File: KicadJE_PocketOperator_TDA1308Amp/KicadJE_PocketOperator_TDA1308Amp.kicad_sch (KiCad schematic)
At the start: 7 parts, among them J101 AudioJack3, J102 AudioJack3, J103 AudioJack3, J104 AudioJack3, J105 AudioJack3, J106 AudioJack3

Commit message: battery power
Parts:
- added C101: C, symbol Device:C
- added SW101: SW_SPST, symbol Switch:SW_SPST
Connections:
- net +BATT: now reaches BT101.1 (+)
- net +BATT: now also C101.1, SW101.1 (A)
- net GND: now reaches BT101.2 (-)
- net GND: now also J101.S, J102.S, J103.S, J104.S, J105.S, J106.S, C101.2
- net Out2R: now reaches J105.R
- net Out2L: now reaches J105.T
- net Out1R: now reaches J104.R
- net Out1L: now reaches J104.T
- net Out3R: now reaches J106.R
- net Out3L: now reaches J106.T
- new net +3V8: SW101.2 (B)
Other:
- moved on the sheet: BT101

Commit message: TDA1308 footprint
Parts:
- added C102: 10u, Resistor_SMD:R_0805_2012Metric_Pad1.20x1.40mm_HandSolder, symbol Device:C
- added D101: LED, LED_SMD:LED_0805_2012Metric_Pad1.15x1.40mm_HandSolder, symbol Device:LED
- added R101: 1k, Resistor_SMD:R_0805_2012Metric_Pad1.20x1.40mm_HandSolder, symbol Device:R
- BT101: footprint (none) -> Battery:BatteryHolder_Keystone_2460_1xAA
- C101: value C -> 1u
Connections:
- net +3V8: now also R101.1
- net GND: now also D101.1 (K)
- new net: D101.2 (A), R101.2

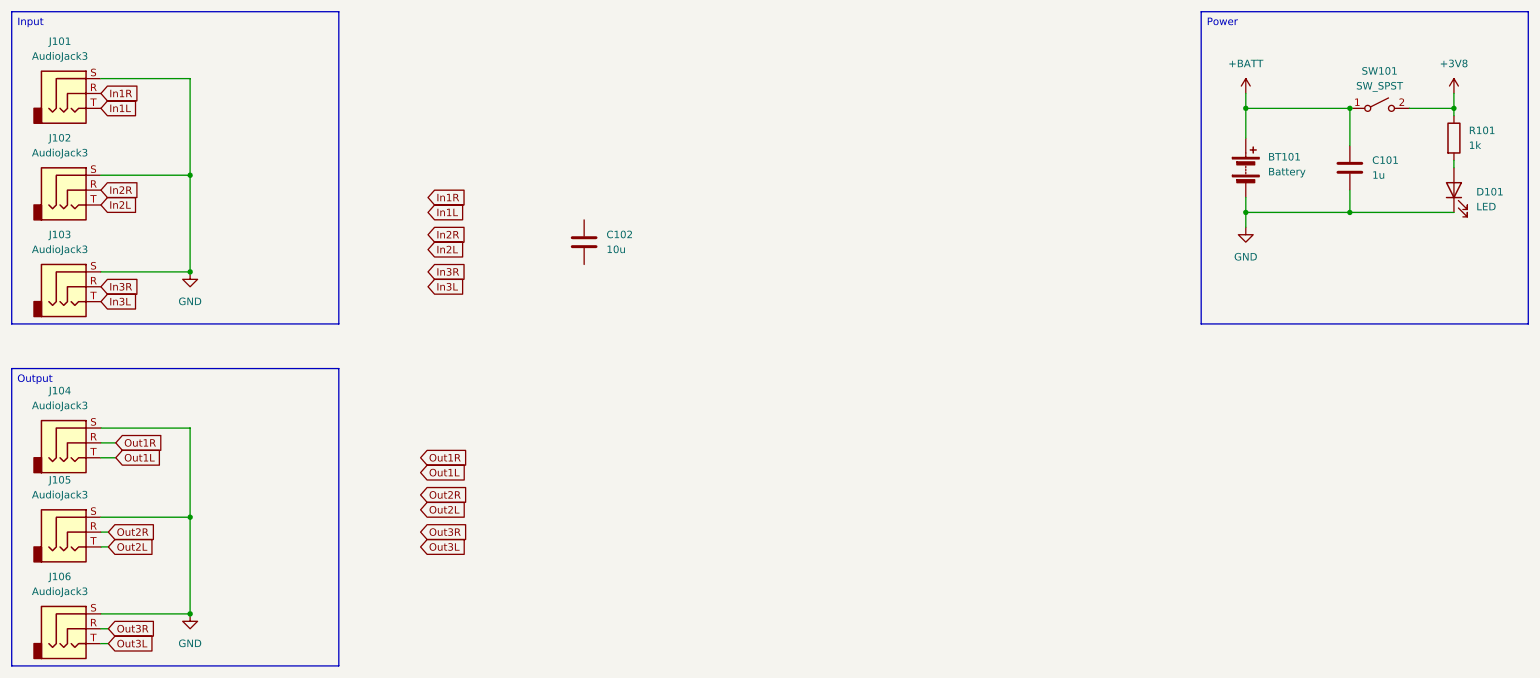
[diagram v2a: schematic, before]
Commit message: TDA1308 symbol
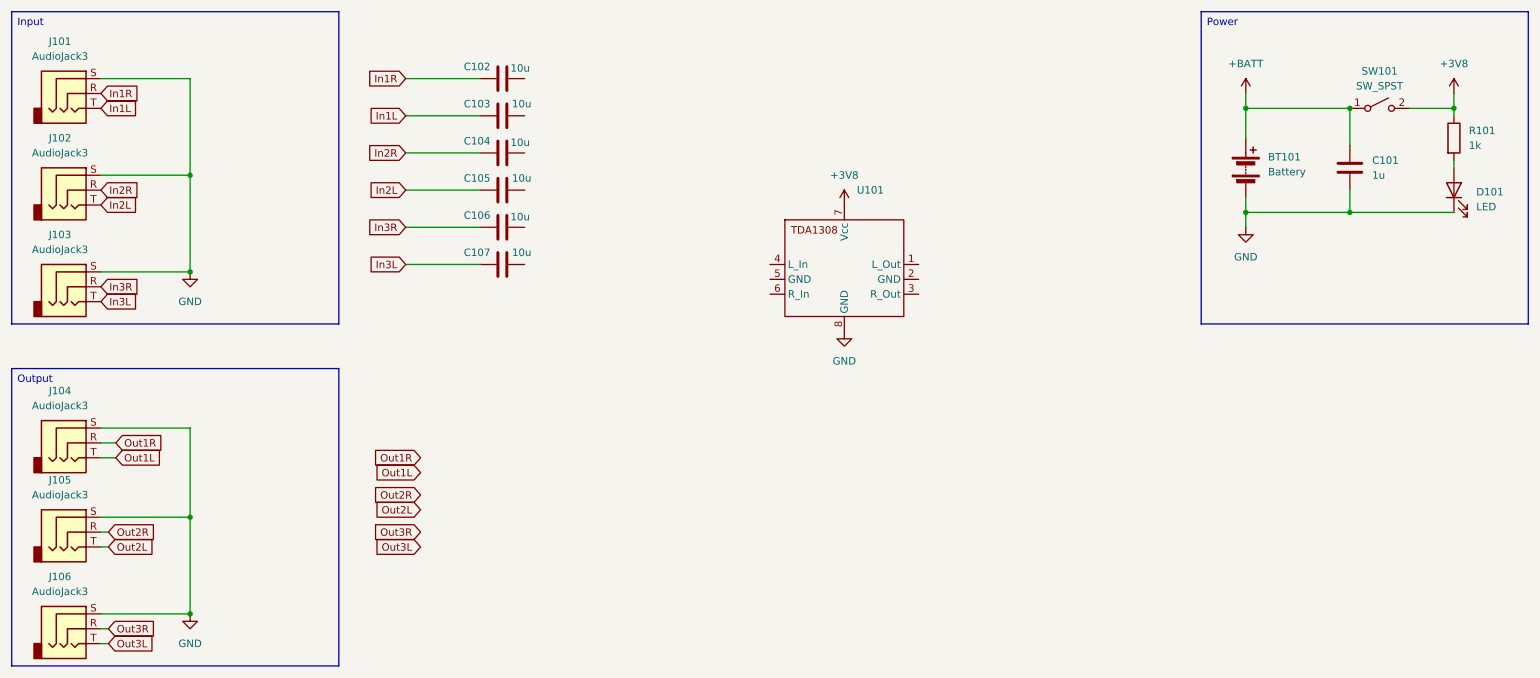
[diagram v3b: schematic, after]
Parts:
- added C103, C104, C105, C106, C107: 10u, Resistor_SMD:R_0805_2012Metric_Pad1.20x1.40mm_HandSolder, symbol Device:C
- added U101: ~, AJ_2025_Library:TDA1308_PCB, symbol AJ_2025:TDA_1308_PCB
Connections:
- net +3V8: now also U101.7 (Vcc)
- net GND: now also U101.8 (GND)
- net In1L: now also C103.1
- net In1R: now also C102.1
- net In2L: now also C105.1
- net In2R: now also C104.1
- net In3L: now also C107.1
- net In3R: now also C106.1
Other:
- moved on the sheet: C102

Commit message: Footprints Updated
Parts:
- added JP101: Out2R, Jumper:SolderJumper-2_P1.3mm_Bridged_RoundedPad1.0x1.5mm, symbol Jumper:Jumper_2_Bridged
- added JP102: Out2L, Jumper:SolderJumper-2_P1.3mm_Bridged_RoundedPad1.0x1.5mm, symbol Jumper:Jumper_2_Bridged
- added JP103: Out3R, Jumper:SolderJumper-2_P1.3mm_Bridged_RoundedPad1.0x1.5mm, symbol Jumper:Jumper_2_Bridged
- added JP104: Out3L, Jumper:SolderJumper-2_P1.3mm_Bridged_RoundedPad1.0x1.5mm, symbol Jumper:Jumper_2_Bridged
- added JP105: InL, Jumper:SolderJumper-2_P1.3mm_Open_RoundedPad1.0x1.5mm, symbol Jumper:Jumper_2_Open
- added JP106: InR, Jumper:SolderJumper-2_P1.3mm_Open_RoundedPad1.0x1.5mm, symbol Jumper:Jumper_2_Open
- added R102, R103, R104, R105, R106, R107: 10k, Resistor_SMD:R_0805_2012Metric_Pad1.20x1.40mm_HandSolder, symbol Device:R
- C101: footprint (none) -> Capacitor_SMD:C_0805_2012Metric_Pad1.18x1.45mm_HandSolder
- J101: value AudioJack3 -> In 1 + Sync; footprint (none) -> Connector_Audio:Jack_3.5mm_PJ311_Horizontal
- J102: value AudioJack3 -> In 2; footprint (none) -> Connector_Audio:Jack_3.5mm_PJ311_Horizontal
- J103: value AudioJack3 -> In 3; footprint (none) -> Connector_Audio:Jack_3.5mm_PJ311_Horizontal
- J104: value AudioJack3 -> Out Stereo; footprint (none) -> Connector_Audio:Jack_3.5mm_PJ311_Horizontal
- J105: value AudioJack3 -> Sync1; footprint (none) -> Connector_Audio:Jack_3.5mm_PJ311_Horizontal
- J106: value AudioJack3 -> Sync2; footprint (none) -> Connector_Audio:Jack_3.5mm_PJ311_Horizontal
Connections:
- net GND: now also U101.2 (GND), U101.5 (GND)
- net In1L: now also JP105.2 (B)
- net In1R: now also JP106.2 (B)
- net Out1L: now also U101.1 (L_Out)
- net Out1R: now also U101.3 (R_Out)
- net Out2L: now also JP102.1 (A)
- net Out2R: now also JP101.1 (A)
- net Out3L: now also JP104.1 (A)
- net Out3R: now also JP103.1 (A)
- net at C104.2: now also R104.1
- net InL: now reaches U101.4 (L_In)
- net InL: now also R103.2, R105.2, R107.2
- net InR: now reaches U101.6 (R_In)
- net InR: now also R102.2, R104.2, R106.2
- net at C103.2: now also R103.1
- net at C105.2: now also R105.1
- net at C107.2: now also R107.1
- net at C106.2: now also R106.1
- net at C102.2: now also R102.1
- new net: JP102.2 (B), JP104.2 (B), JP105.1 (A)
- new net: JP101.2 (B), JP103.2 (B), JP106.1 (A)

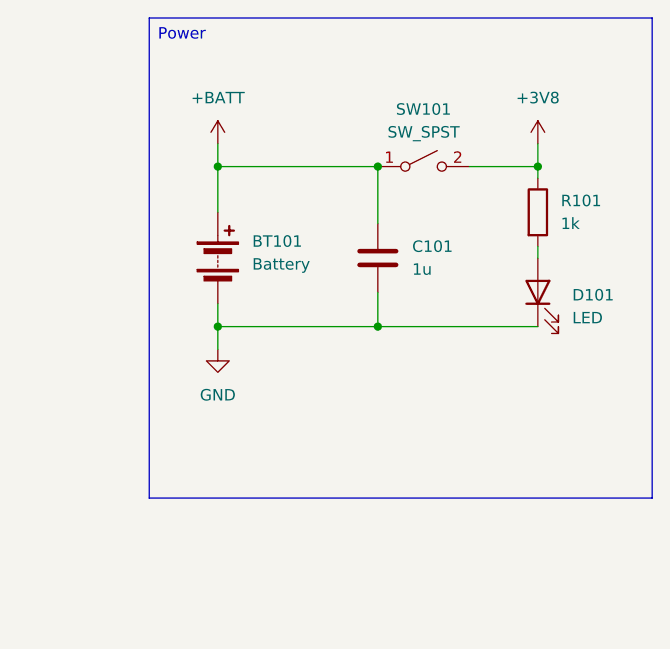
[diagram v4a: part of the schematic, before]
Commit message: footprints placed
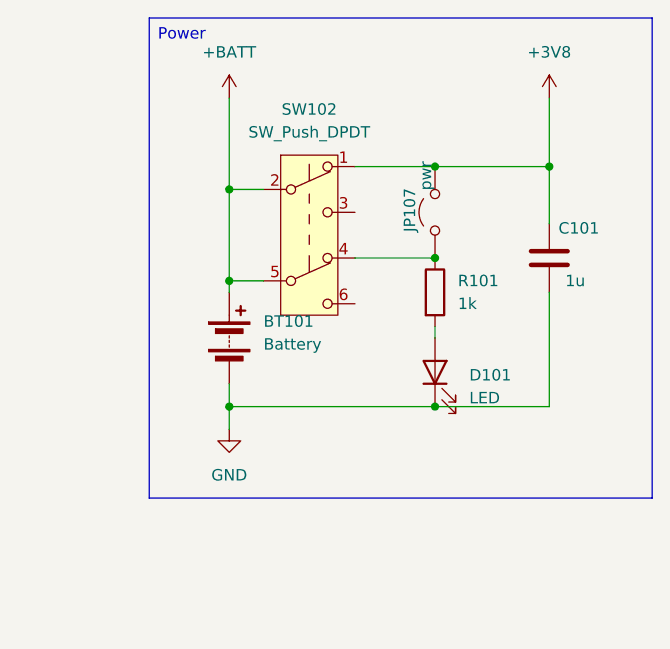
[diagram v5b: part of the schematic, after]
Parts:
- removed SW101: SW_SPST, symbol Switch:SW_SPST
- added JP107: pwr, Jumper:SolderJumper-2_P1.3mm_Open_RoundedPad1.0x1.5mm, symbol Jumper:Jumper_2_Open
- added SW102: SW_Push_DPDT, Button_Switch_THT:SW_Push_2P2T_Toggle_CK_PVA2OAH5xxxxxxV2, symbol Switch:SW_Push_DPDT
- BT101: footprint Battery:BatteryHolder_Keystone_2460_1xAA -> AJ_2025_Library:BatteryHolder_1xAA
- J101, J102, J103, J104, J105, J106: footprint Connector_Audio:Jack_3.5mm_PJ311_Horizontal -> Connector_Audio:Jack_3.5mm_Lumberg_1503_07_Horizontal
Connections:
- net +3V8: now also C101.1, JP107.2 (B), SW102.1 (A); no longer R101.1
- net +BATT: now also SW102.2 (B), SW102.5 (B); no longer C101.1
- new net: JP107.1 (A), R101.1, SW102.4 (A)
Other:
- moved on the sheet: BT101, C101, D101, R101

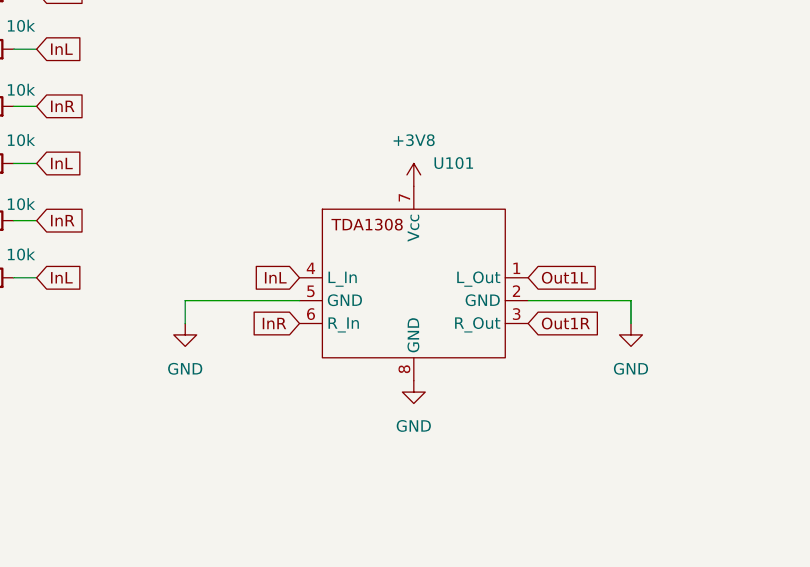
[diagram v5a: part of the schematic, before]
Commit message: Logo etc
TDA symbol PSU GND swapped
New logos
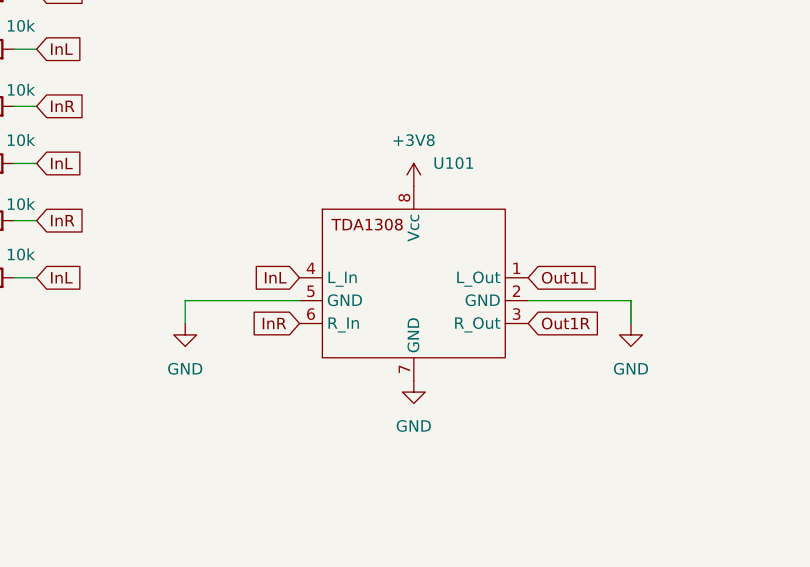
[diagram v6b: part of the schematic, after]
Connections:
- net +3V8: now also U101.8 (Vcc); no longer U101.7 (Vcc)
- net GND: now also U101.7 (GND); no longer U101.8 (GND)
